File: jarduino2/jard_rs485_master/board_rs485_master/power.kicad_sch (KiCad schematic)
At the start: 15 parts, among them J1 POWER_12V, J2 ON_OFF, J5 Leds RGB, Q3 BC327, U2 BPC_Alim5V

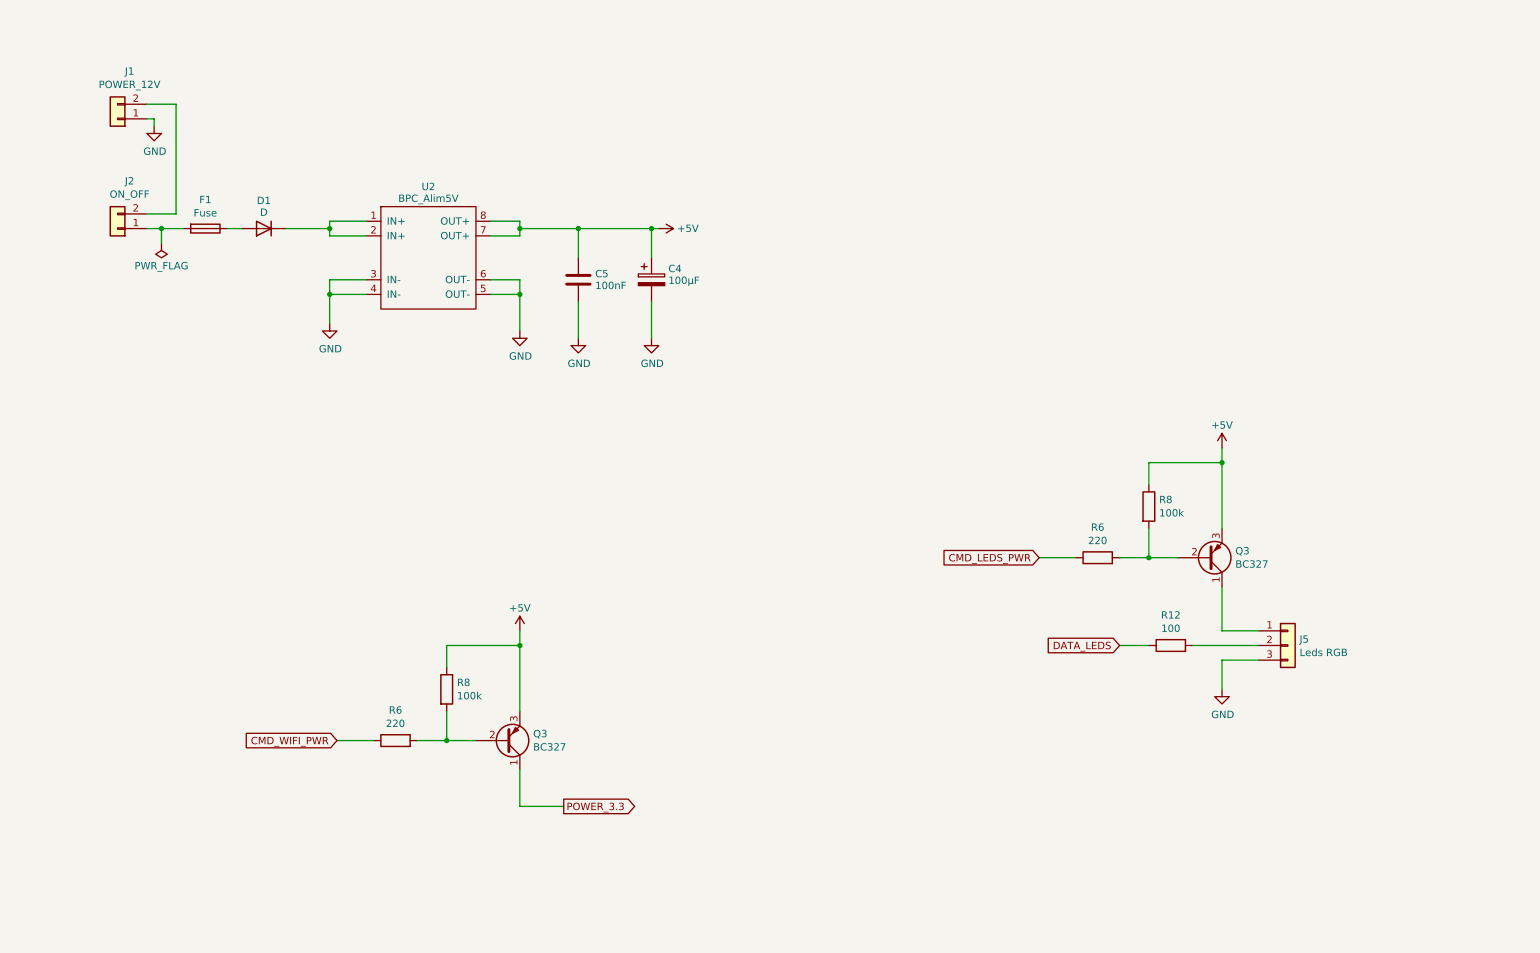
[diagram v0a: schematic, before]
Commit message: Candidate pour revue du master Oyas (avec modules en tant que shield MEGA)
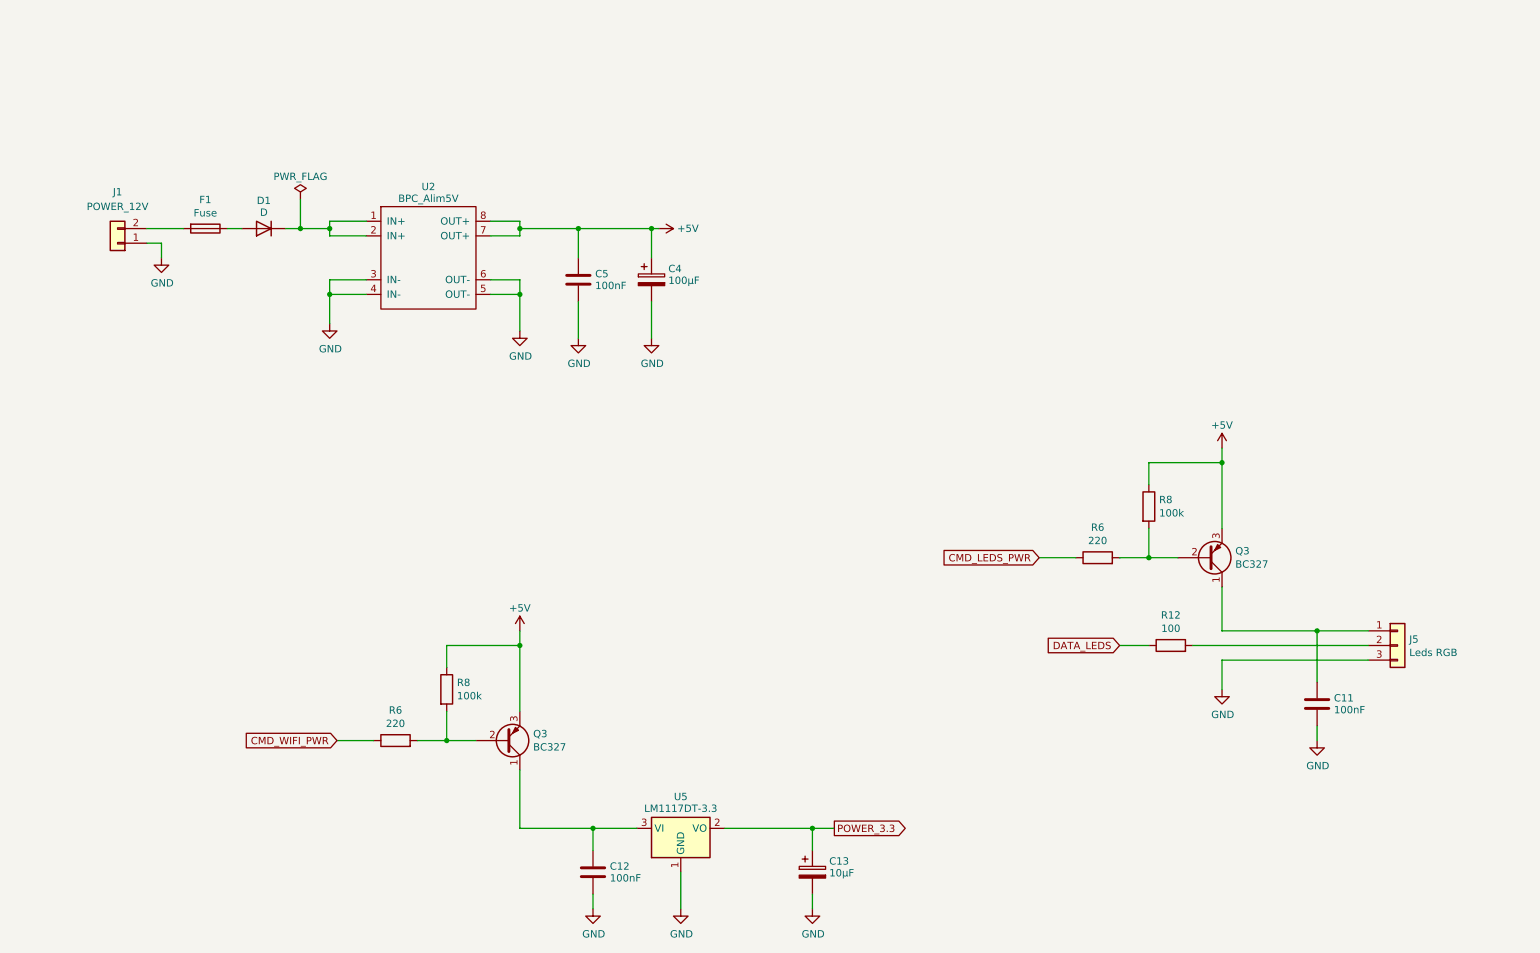
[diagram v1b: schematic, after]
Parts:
- removed J2: ON_OFF, TerminalBlock_Phoenix:TerminalBlock_Phoenix_MKDS-1,5-2-5.08_1x02_P5.08mm_Horizontal, symbol Connector_Generic:Conn_01x02
- added C11, C12: 100nF, Capacitor_THT:C_Disc_D5.0mm_W2.5mm_P2.50mm, symbol Device:C
- added C13: 10µF, Capacitor_THT:CP_Radial_D4.0mm_P2.00mm, symbol Device:C_Polarized
- added U5: LM1117DT-3.3, Package_TO_SOT_THT:TO-220-3_Vertical, symbol Regulator_Linear:LM1117DT-3.3
- C4: footprint Capacitor_THT:C_Disc_D5.0mm_W2.5mm_P2.50mm -> Capacitor_THT:CP_Radial_D8.0mm_P3.80mm
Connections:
- net GND: now also C11.2, C12.2, C13.2, U5.1 (GND)
- net POWER_3.3: now also C13.1, U5.2 (VO); no longer Q3.1 (C)
- net at F1.2: now also J1.2 (Pin_2)
- net at J5.1 (Pin_1), Q3.1 (C): now also C11.1
- new net: C12.1, Q3.1 (C), U5.3 (VI)
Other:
- company: (none) -> BPC
- title: (none) -> Commande des OYA - Maître RS485
- moved on the sheet: J1, J5

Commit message: Finalisation dossier
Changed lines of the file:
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@@
   (title_block
     (title "Commande des OYA - Maître RS485")
-    (date "2024-03-30")
+    (date "2024-03-31")
     (rev "A0")
     (company "BPC")
@@
   )
   (wire (pts (xy 240.03 124.46) (xy 223.52 124.46))
+    (stroke (width 0) (type default))
+  )
+  (wire (pts (xy 114.3 154.94) (xy 114.3 158.75))
     (stroke (width 0) (type default))
   )
@@
         )
       )
+    )
+  )
+  (symbol (lib_id "power:PWR_FLAG") (at 114.3 154.94 0) (unit 1)
+    (in_bom yes) (on_board yes) (dnp no) (fields_autoplaced)
+    (property "Reference" "#FLG03" (at 114.3 153.035 0)
+      (effects (font (size 1.27 1.27)) hide)
+    )
+    (property "Value" "PWR_FLAG" (at 114.3 150.995 0)
+      (effects (font (size 1.27 1.27)))
+    )
+    (property "Footprint" "" (at 114.3 154.94 0)
+      (effects (font (size 1.27 1.27)) hide)
+    )
+    (property "Datasheet" "~" (at 114.3 154.94 0)
+      (effects (font (size 1.27 1.27)) hide)
+    )
+    (pin "1")
+    (instances
+      (project "board_rs485_master"
+        (path "/27904310-f1aa-47e2-a2a6-8db936442bd1/2eaa2441-998c-4f1a-b526-09e479f565d5"
+          (reference "#FLG03") (unit 1)
+        )
+      )

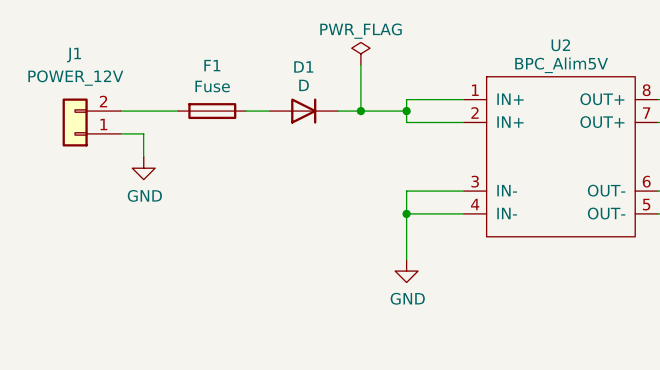
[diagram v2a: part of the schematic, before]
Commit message: Amélioration suite remise en route:
  - Agrandissement trous des LEDs D1 et D3
  - Correction erreur type du MOS P GDS
  - Agrandissement empreintes de R5,R7,R13 et R10 + verticales
  - Ajout de la description des opérations de rework pour le MOD485
  - Ajout d'une interface pour adapter le bus (5V, A, B et Gnd)
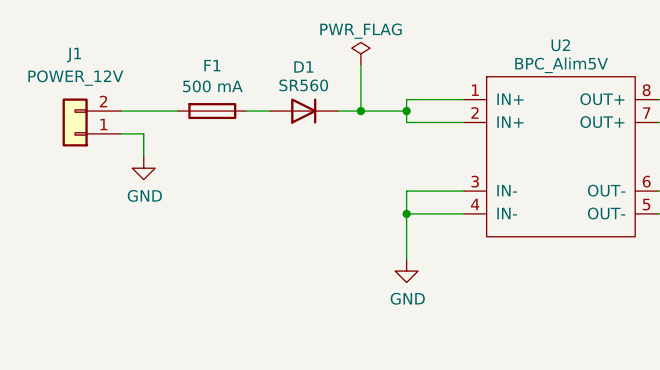
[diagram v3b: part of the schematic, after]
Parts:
- D1: value D -> SR560; footprint Diode_THT:D_A-405_P2.54mm_Vertical_AnodeUp -> Diode_THT:D_DO-15_P2.54mm_Vertical_AnodeUp
- F1: value Fuse -> 500 mA
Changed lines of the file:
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@@
   (title_block
     (title "Commande des OYA - Maître RS485")
-    (date "2024-03-31")
-    (rev "A0")
+    (date "2024-04-09")
+    (rev "B0")
     (company "BPC")
     (comment 1 "Extension Wifi (ESP01)")
@@
       (effects (font (size 1.27 1.27)))
     )
-    (property "Value" "D" (at 57.15 51.808 0)
-      (effects (font (size 1.27 1.27)))
-    )
-    (property "Footprint" "Diode_THT:D_A-405_P2.54mm_Vertical_AnodeUp" (at 57.15 54.61 0)
+    (property "Value" "SR560" (at 57.15 51.808 0)
+      (effects (font (size 1.27 1.27)))
+    )
+    (property "Footprint" "Diode_THT:D_DO-15_P2.54mm_Vertical_AnodeUp" (at 57.15 54.61 0)
       (effects (font (size 1.27 1.27)) hide)
     )
@@
       (effects (font (size 1.27 1.27)))
     )
-    (property "Value" "Fuse" (at 46.99 51.9176 90)
-      (effects (font (size 1.27 1.27)))
-    )
+    (property "Value" "500 mA" (at 46.99 51.9176 90)
+      (effects (font (size 1.27 1.27)))
+    )

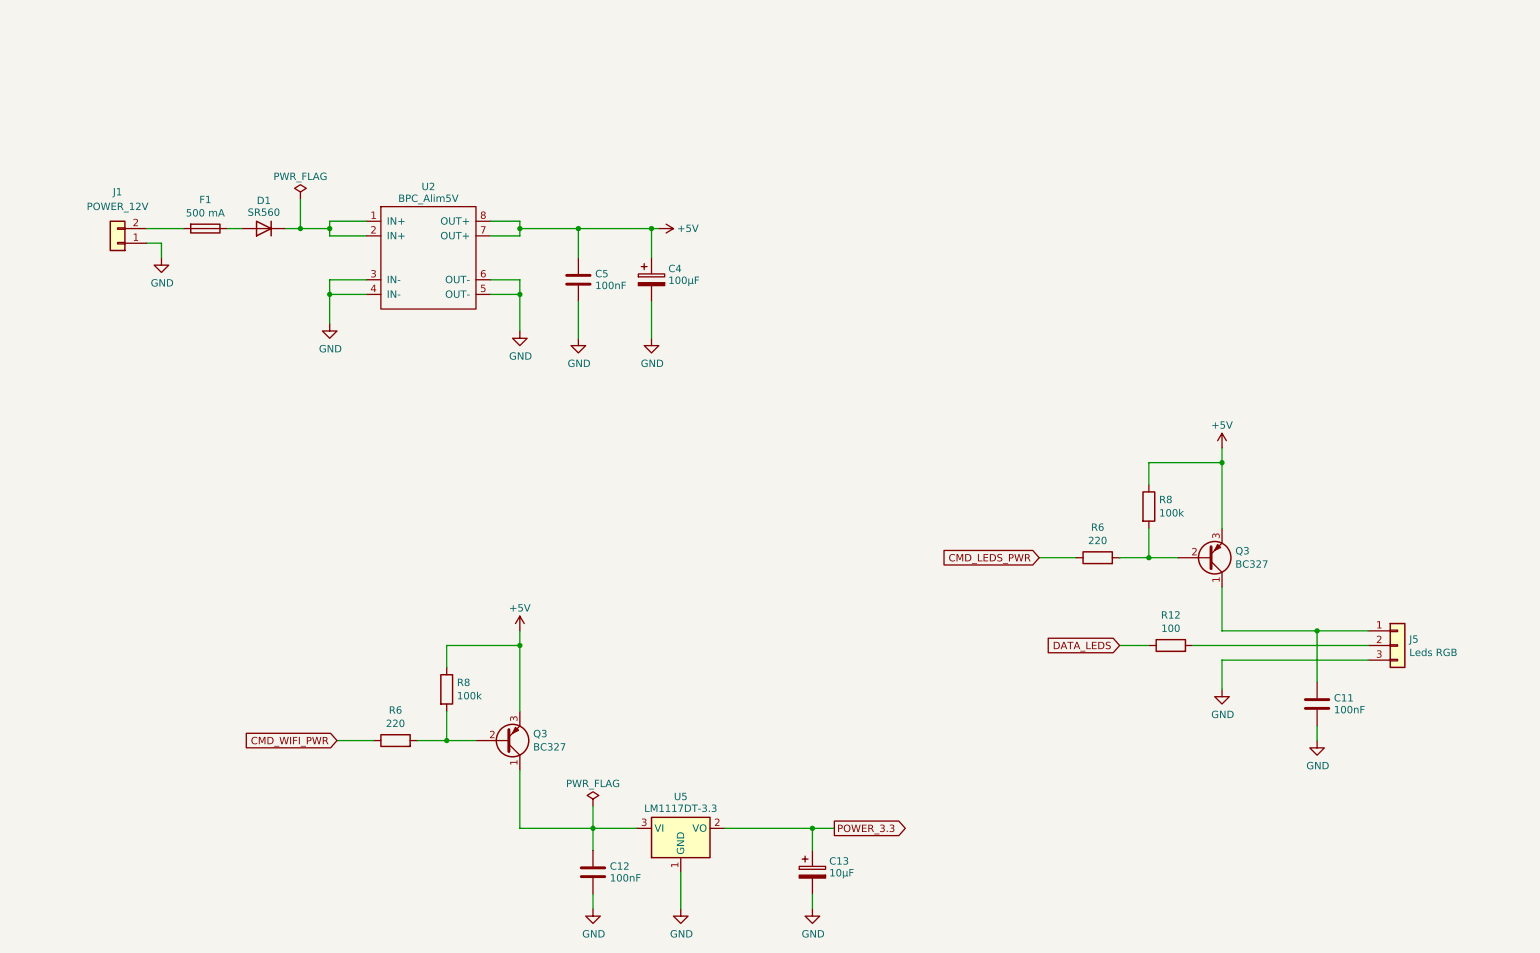
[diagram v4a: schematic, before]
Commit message: Changement de la logique de commande des PWR Wifi et LEDs (avec un npn en plus)
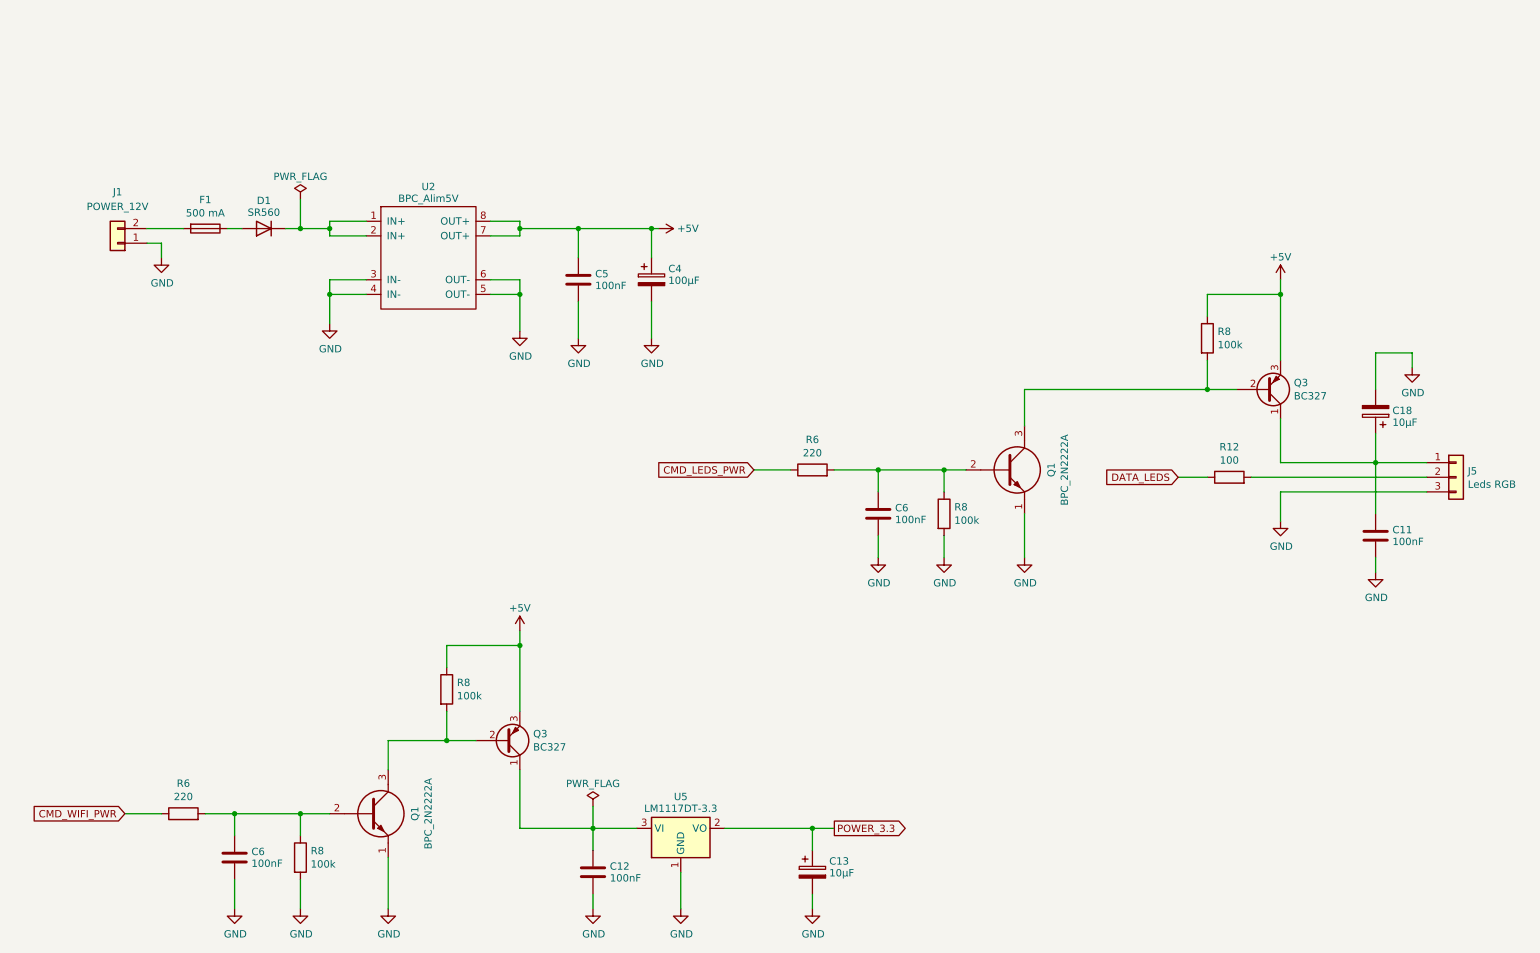
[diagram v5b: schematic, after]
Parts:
- added C18: 10µF, Capacitor_THT:CP_Radial_D4.0mm_P2.00mm, symbol Device:C_Polarized
- added C6 (x2): 100nF, Capacitor_THT:C_Disc_D5.0mm_W2.5mm_P2.50mm, symbol Device:C
- added Q1 (x2): BPC_2N2222A, Package_TO_SOT_THT:TO-92, symbol bpc:BPC_2N2222A
- added R8 (x2): 100k, Resistor_THT:R_Axial_DIN0204_L3.6mm_D1.6mm_P7.62mm_Horizontal, symbol Device:R
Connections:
- net GND: now also C18.2, C6.2, C6.2, Q1.1, Q1.1, R8.2, R8.2
- net at C11.1, J5.1 (Pin_1), Q3.1 (C): now also C18.1
- net at Q3.2 (B), R8.2: now also Q1.3; no longer R6.2 (x2)
- new net: C6.1, Q1.2, R6.2, R8.1 (x2)
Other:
- moved on the sheet: C11, J5, Q3, R12, R6, R8

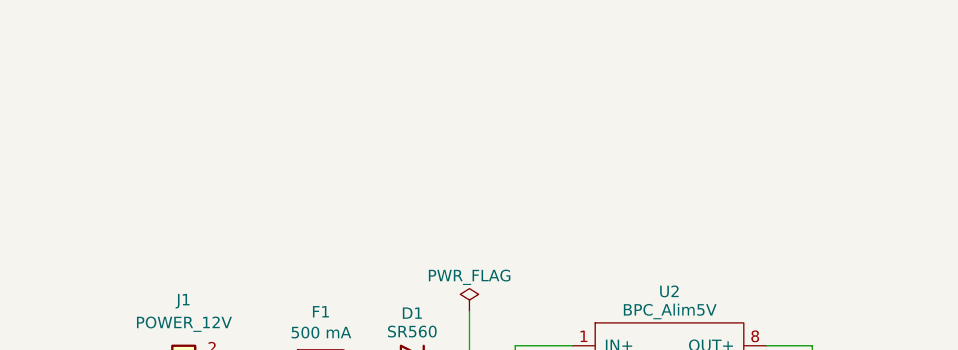
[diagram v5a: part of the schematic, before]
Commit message: Titres + finitions (vias)
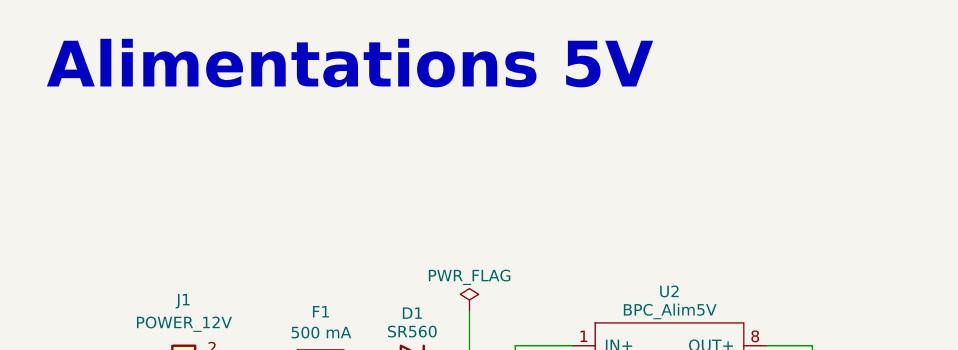
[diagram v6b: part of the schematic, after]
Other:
- note added: "Alimentations 5V"
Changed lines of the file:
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@@
     (stroke (width 0) (type default))
+  )
+  (text "Alimentations 5V" (at 16.51 25.4 0)
+    (effects (font (size 5.08 5.08) (thickness 2.54) bold) (justify left bottom))
   )
   (global_label "DATA_LEDS" (shape input) (at 215.9 97.79 180)
